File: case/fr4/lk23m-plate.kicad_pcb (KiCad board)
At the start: 2 copper layers, 76.2 x 119.1 mm, 8 parts

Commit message: Model should be done, we should just look at exporting keyboard.pretty as a library
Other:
- outline, holes or cut-outs redrawn

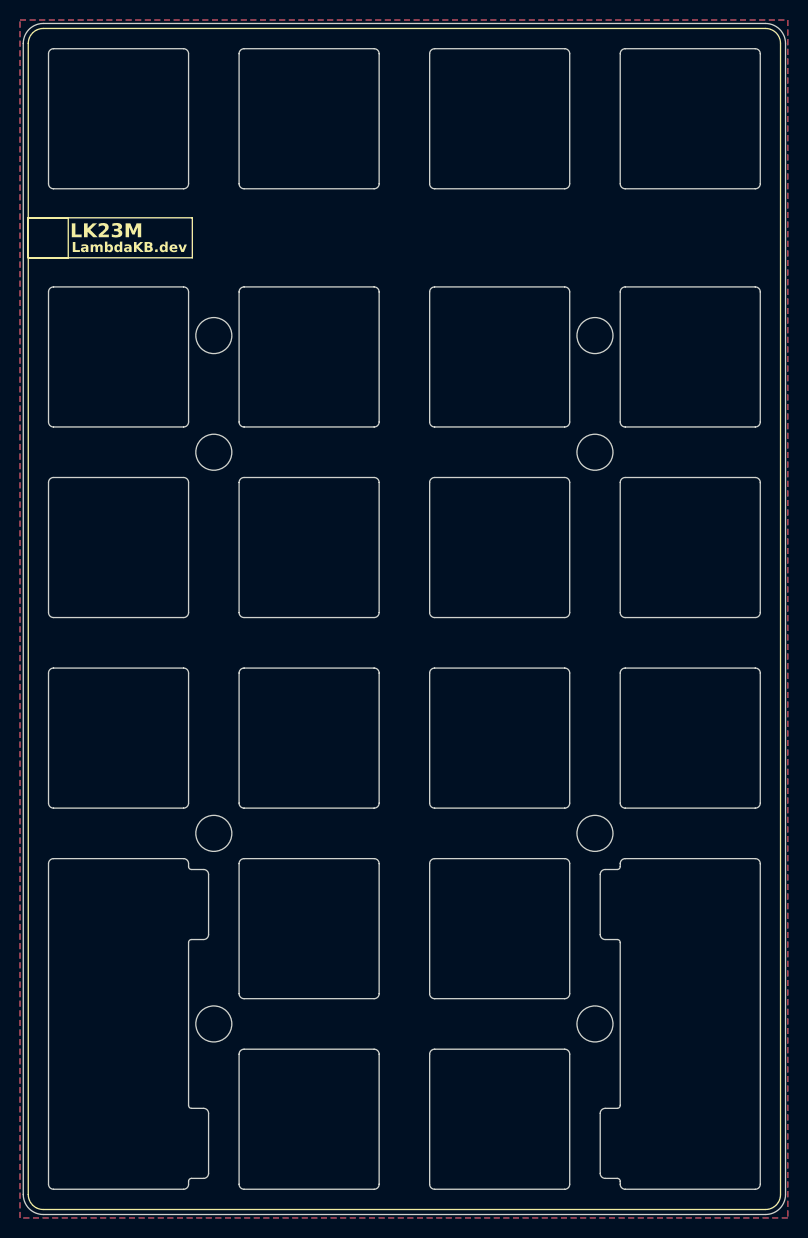
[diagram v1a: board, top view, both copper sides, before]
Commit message: Move KiBot config to reusable folder and fix PCBDraw output
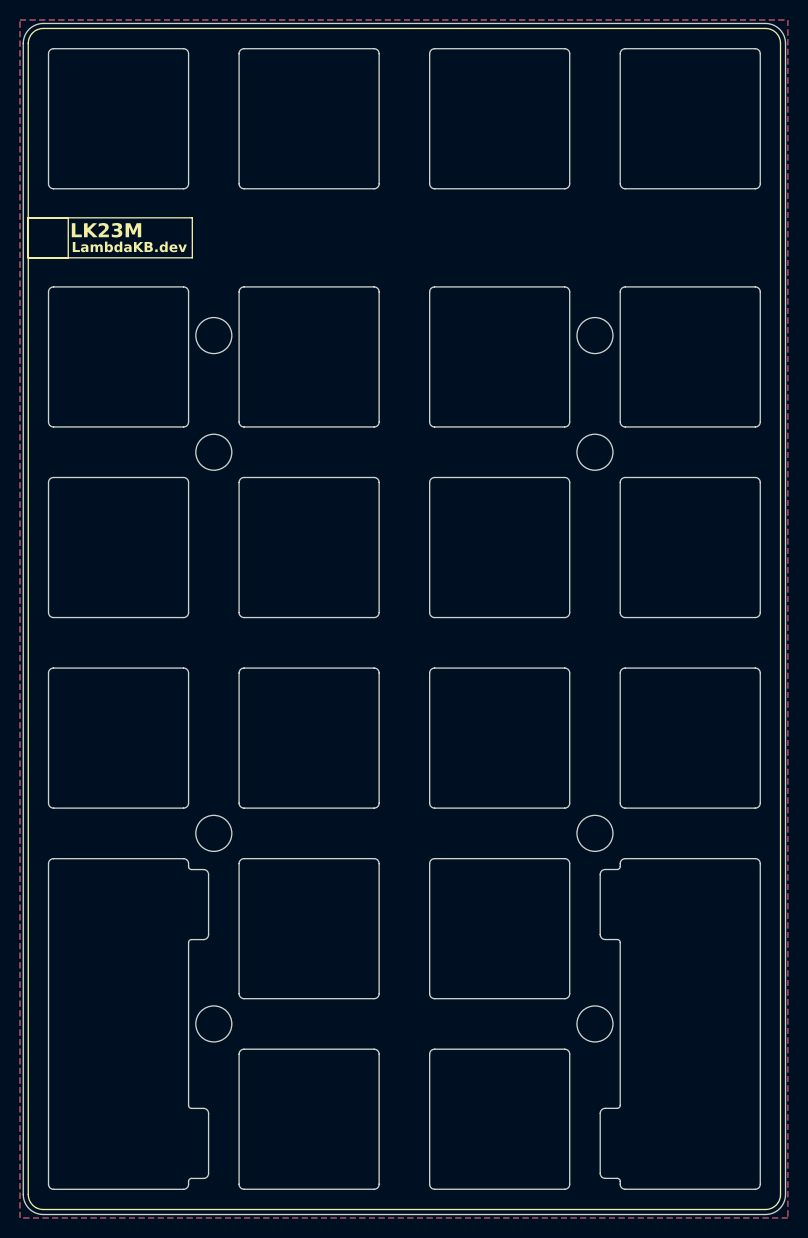
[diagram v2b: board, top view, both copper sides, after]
